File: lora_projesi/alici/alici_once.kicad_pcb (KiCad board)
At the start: 4 copper layers, 88 x 102 mm, 127 parts, among them J1 USB-C, J2 SMA, J3 RJ45, J4 u.FL (ANA ANTEN), J5 12 V GIRIS, J6 LAMBA, J7 MICRO-SIM, J8 u.FL (YARDIMCI ANTEN, ISTEGE 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, K1 SRD-12VDC-SL-A, Q1 AO3401A, Q2 MMBT2222A, Q3 MMBT2222A, Q4 MMBT2222A, SW1 DUGME, U1 ESP32-S3-WROOM-1-N4, U10 SIM7600SA, U11 AP2112K-3.3, U12 ESDA6V1-5SC6, U4 RFM95W-915S2, U5 TPS62933DRLR, U6 TPS62933DRLR, U7 USBLC6-2SC6, U8 TXB0104PW, U9 W5500, Y1 25 MHz

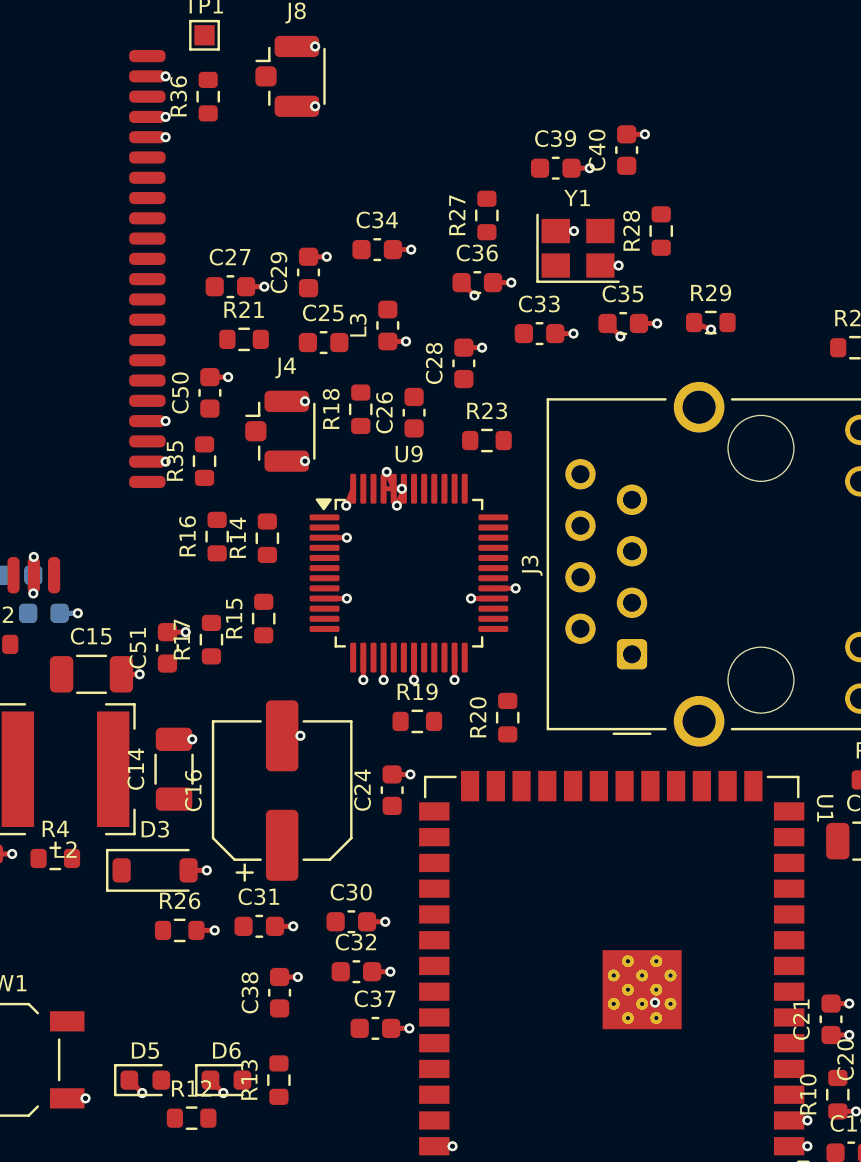
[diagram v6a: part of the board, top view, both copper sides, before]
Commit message: Alici: ETH dekuplaj kondansatorleri arka yuze (boru hatti suruyor)
Co-Authored-By: Claude Sonnet 5.5 <noreply@anthropic.com>
Claude-Session: https://claude.ai/code/session_01Q71gHQtKJ86ZE2CtYTYSwP
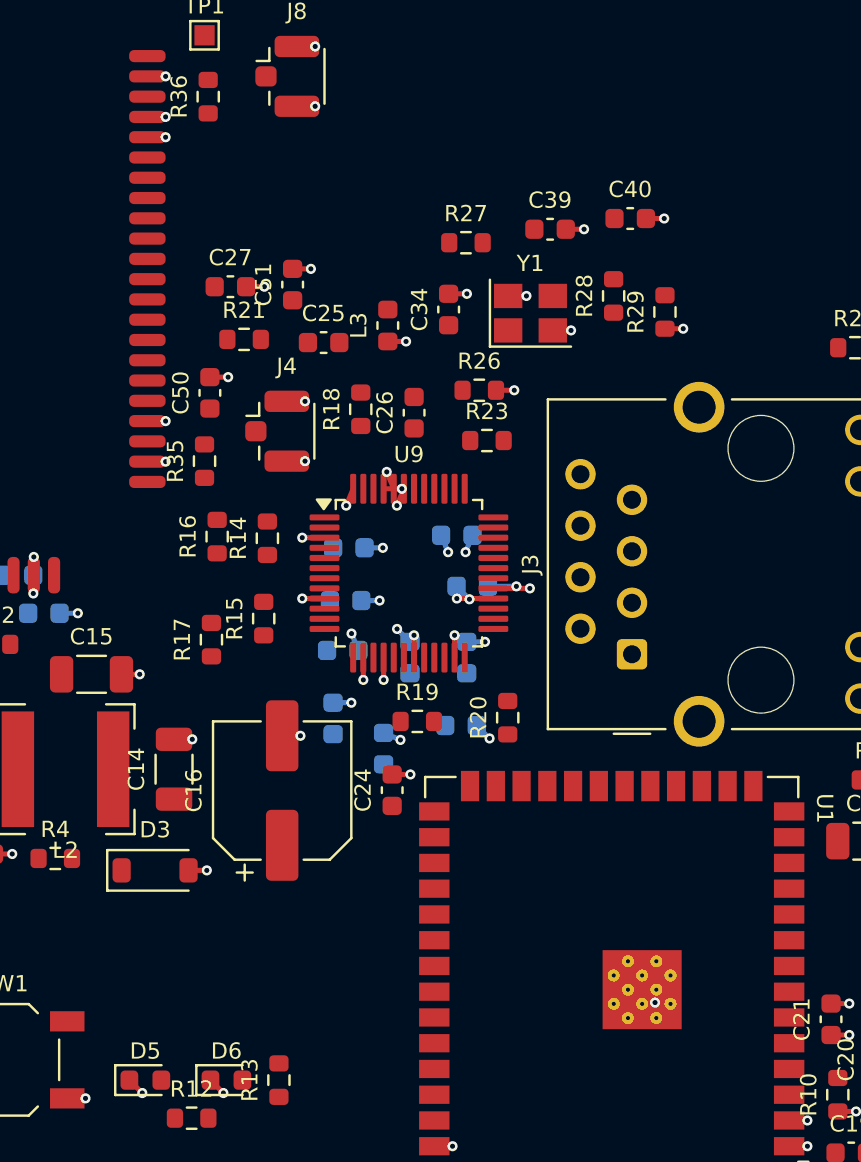
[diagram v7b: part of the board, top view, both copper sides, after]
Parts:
- C28, C29, C30, C31, C32, C33, C35, C36, C37, C38: moved to B.Cu
- moved R26 30.5 mm to (59.5, 53.0)
- moved C33 19.7 mm to (58.6, 69.5)
- moved C51 19.0 mm to (50.3, 47.8)
- moved C32 16.4 mm to (58.9, 66.2), turned to 90 degrees
- moved C29 16.3 mm to (52.9, 63.4), turned to 0 degrees
- moved C31 15.2 mm to (56.0, 66.2), turned to 90 degrees
- moved C35 14.9 mm to (59.1, 62.6)
- moved C37 13.8 mm to (54.7, 70.7), turned to 90 degrees
- moved C38 13.8 mm to (52.3, 69.2)
- moved C30 13.4 mm to (52.7, 65.8)
- moved C36 12.5 mm to (58.4, 60.1)
- moved C28 10.7 mm to (53.0, 60.8), turned to 0 degrees
- moved C34 4.60 mm to (58.0, 49.0), turned to 90 degrees
- moved R28 3.97 mm to (66.1, 48.3)
- moved Y1 3.97 mm to (62.0, 49.2)
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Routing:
- net GND: track 111.8 -> 113.0 mm
- net +3V3: track 25.8 -> 26.5 mm

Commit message: Alici: kristal arka yuz, plane via ic tarafa, boru hatti yeniden
Co-Authored-By: Claude Sonnet 5.5 <noreply@anthropic.com>
Claude-Session: https://claude.ai/code/session_01Q71gHQtKJ86ZE2CtYTYSwP
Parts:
- C39, C40, R27, R28, Y1: moved to B.Cu
- moved C39 12.7 mm to (53.0, 52.9), turned to 90 degrees
- moved R27 12.2 mm to (53.9, 56.9), turned to 90 degrees
- moved R28 10.5 mm to (56.8, 53.3), turned to 0 degrees
- moved C40 9.60 mm to (60.8, 51.9), turned to 90 degrees
- moved Y1 8.64 mm to (57.8, 56.7)
- moved R29 7.24 mm to (61.5, 50.3), turned to 0 degrees
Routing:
- net GND: track 113.0 -> 113.5 mm
